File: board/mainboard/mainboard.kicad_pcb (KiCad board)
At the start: 2 copper layers, 147.5 x 50 mm, 108 parts, among them J1 BACKL, K1 IRDA_EN, P1 I2C, P10 BUMPERS, P11 CPLD_JTAG, P12 POWER, P13 UART, P14 AUDIO, P15 MIC, P2 Motor1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

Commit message: Apparently I forgot to save the most recent changes
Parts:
- C17: value 0.47uF -> 470nF
- C20: value 2.2nF -> 2.2uF
- C23: value 1uF -> 1.0uF
- C24: value 1uF -> 0.1uF
- C25: value 0.1uF -> 1uF
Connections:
- C20 pad 1: GND -> (no net)

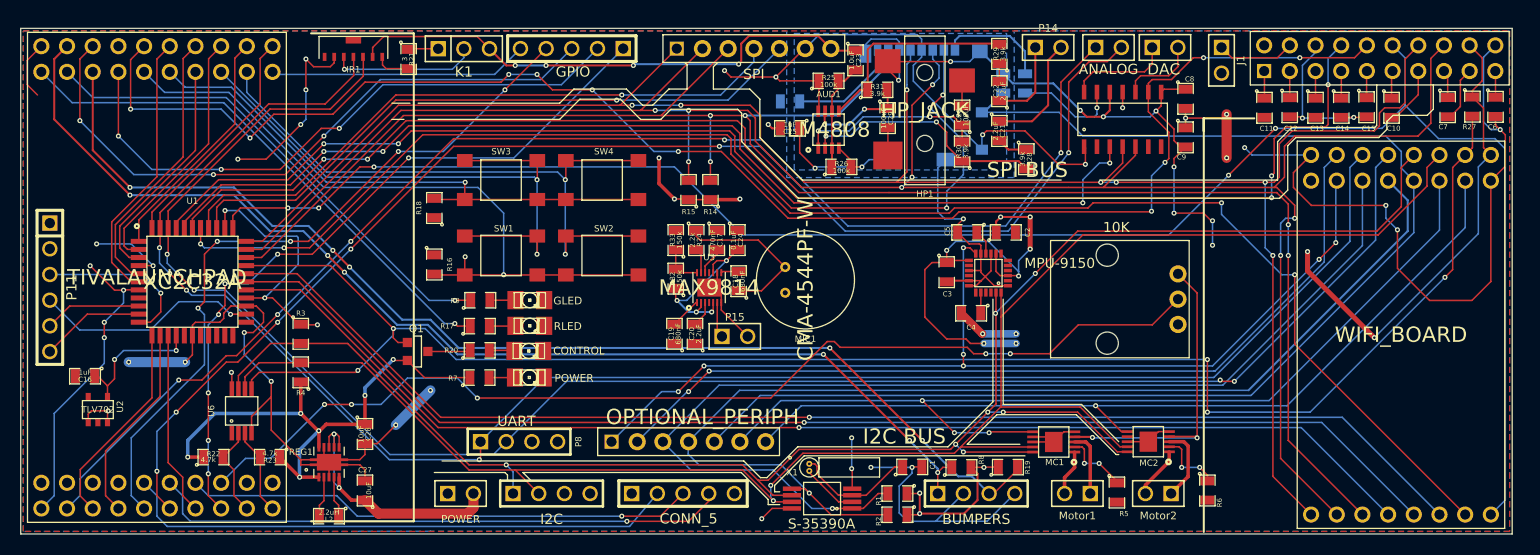
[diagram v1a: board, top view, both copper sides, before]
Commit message: Full rework of all the silk screen, including bus labels, header labels, chip labels
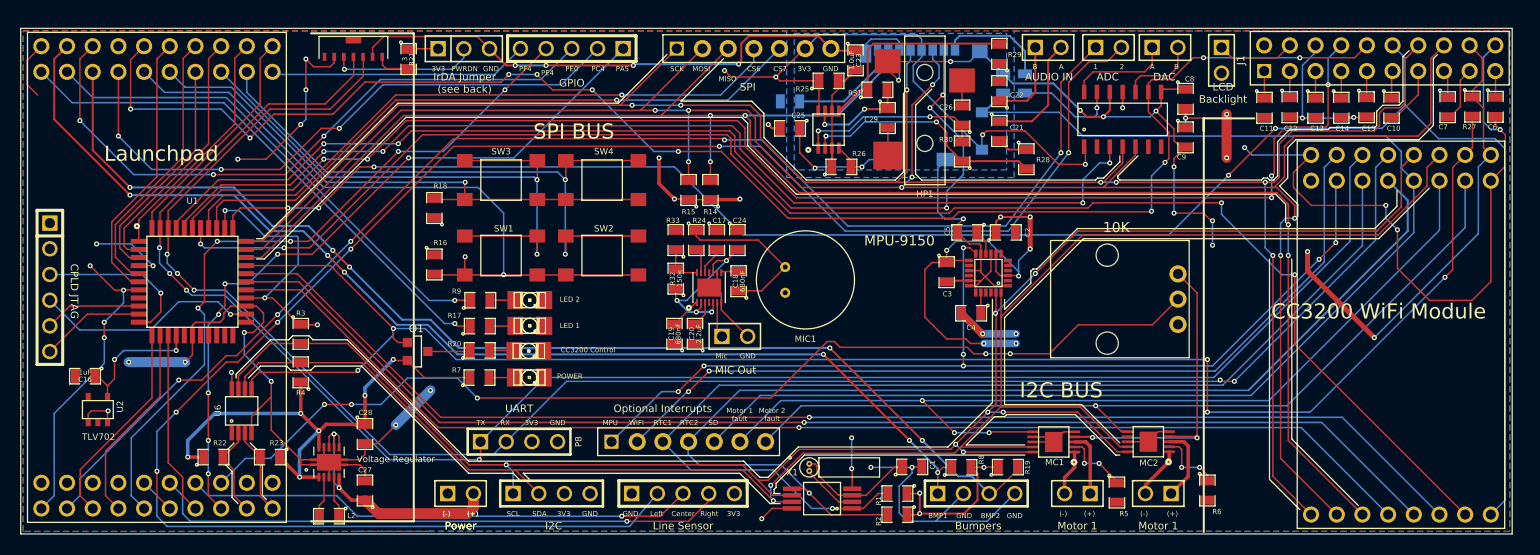
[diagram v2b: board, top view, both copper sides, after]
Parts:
- P4: value SPI -> dSPI
- P5: value DAC -> dDAC
- Voltage Regulator: renamed from REG1
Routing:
- net N-00000116: track 27.5 -> 38.6 mm
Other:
- board text added: "(+)"
- board text added: "(-)"
- board text added: "1"
- board text added: "2"
- board text added: "3V3"
- board text added: "A"
- board text added: "ADC"
- board text added: "AUDIO IN"
- board text added: "B"
- board text added: "BMP1"
- board text added: "BMP2"
- board text added: "Bumpers"
- board text added: "CC3200 Control"
- board text added: "CC3200 WiFi Module"
- board text added: "CPLD JTAG"
- board text added: "CS6"
- board text added: "CS7"
- board text added: "Center"
- board text added: "DAC"
- board text added: "GND"
- board text added: "GPIO"
- board text added: "I2C"
- board text added: "IrDA Jumper (see back)"
- board text added: "IrDA Module Jumper Note: Connecting PWRDN to 3V3 powers on the IrDA Module. Connecting PWRDN to GND powers off the IrDA Module."
- board text added: "LCD Backlight"
- board text added: "LED 1"
- board text added: "LED 2"
- board text added: "Launchpad"
- board text added: "Left"
- board text added: "Line Sensor"
- board text added: "MIC Out"
- board text added: "MISO"
- board text added: "MOSI"
- board text added: "MPU"
- board text added: "Mic"
- board text added: "Motor 1"
- board text added: "Motor 1 fault"
- board text added: "Motor 2 fault"
- board text added: "Optional Interrupts"
- board text added: "PA5"
- board text added: "PC4"
- board text added: "PE0"
- board text added: "PE4"
- board text added: "PF4"
- board text added: "POWER"
- board text added: "PWRDN"
- board text added: "Power"
- board text added: "RTC1"
- board text added: "RTC2"
- board text added: "RX"
- board text added: "Right"
- board text added: "SCK"
- board text added: "SCL"
- board text added: "SD"
- board text added: "SDA"
- board text added: "SPI"
- board text added: "TX"
- board text added: "UART"
- board text added: "WIFI"

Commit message: fixed DRC errors on schematic
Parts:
- P4: value dSPI -> SPI
- P5: value dDAC -> DAC
- REG1: renamed from Voltage Regulator
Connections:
- C20 pad 1: (no net) -> GND
